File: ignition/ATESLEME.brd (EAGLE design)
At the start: 34.6 x 56.6 mm, 54 parts, among them U1 ADXL345PATRICK, U3 AMS1117-3.3

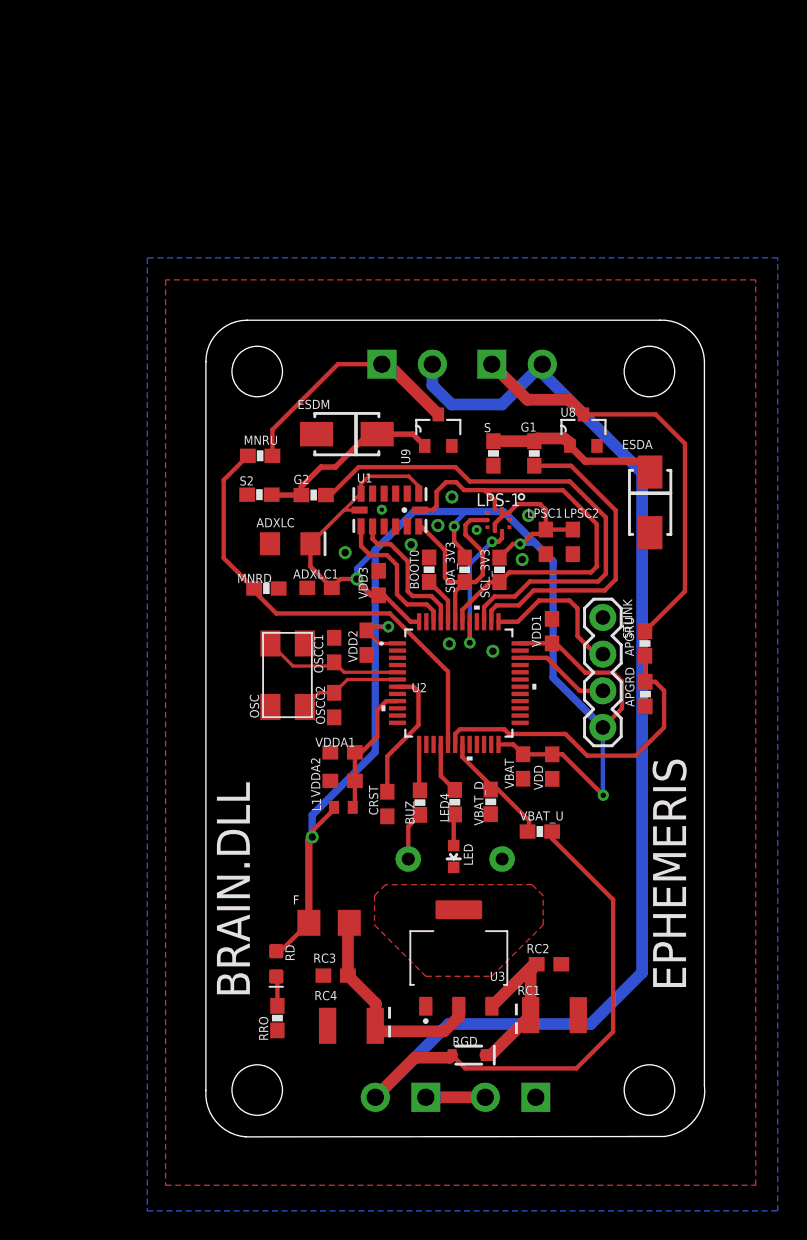
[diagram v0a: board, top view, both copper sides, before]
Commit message: Extra polygon was added for methal distance
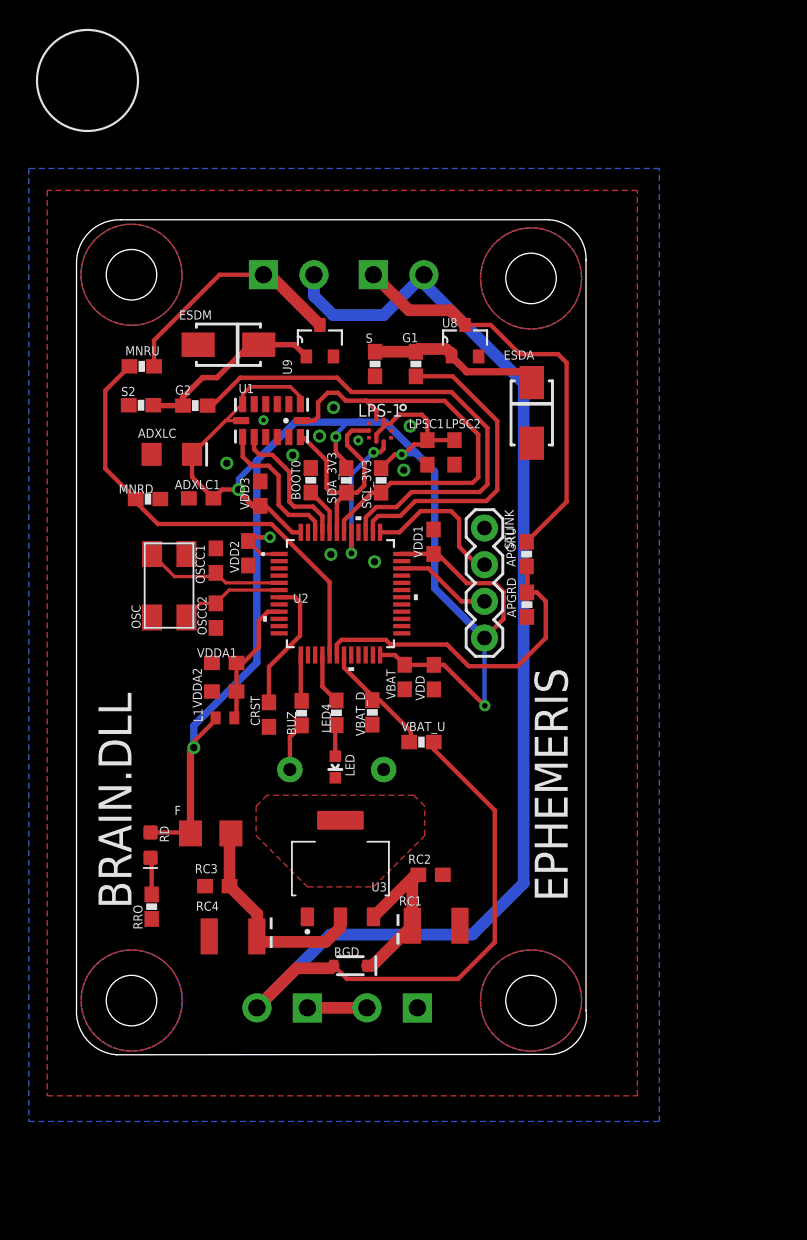
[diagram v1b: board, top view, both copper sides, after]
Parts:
- moved RD 12.0 mm to (-1.04, 21.0)
- moved RRO 11.6 mm to (-0.97, 16.8)
- moved APGRD 10.3 mm to (25.0, 37.7)
- moved ADXLC1 10.3 mm to (2.46, 45.1)
- moved APGRU 10.3 mm to (25.0, 41.2)
- moved APOGEE 10.3 mm to (14.4, 60.6)
- moved BUZ 10.3 mm to (9.42, 30.2)
- moved ESDA 10.3 mm to (25.4, 51.0)
- moved ESDM 10.3 mm to (4.36, 55.7)
- moved F 10.3 mm to (3.12, 21.8)
- moved G1 10.3 mm to (17.3, 54.4)
- moved LED 10.3 mm to (11.8, 26.4)
- moved LED4 10.3 mm to (11.8, 30.2)
- moved LPSC1 10.3 mm to (18.1, 48.2)
- moved LPSC2 10.3 mm to (20.0, 48.2)
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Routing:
- net N$2: track 2.06 -> 2.57 mm
- added copper zone on layer 1, net D
- added copper zone on layer 16, net D
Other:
- board size 34.6 x 56.6 mm -> 35.3 x 57.9 mm

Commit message: Redesign was maken for ignition
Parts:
- removed OSC: (no value), ABMM2-8.000MHZ-E2-T:ABMM2-8.000MHZ-E2-T
- added Y2: ABM2B-8.000MHZ-10-1-U-T, ABM3B-26.000MHZ-10-1-U-T:OSCCC500X320X110-4N
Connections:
- net GND: now also Y2.2, Y2.4
- net OSC_OUT: now also Y2.3; no longer OSC.OUT
- net OSC_ıN: now also Y2.1; no longer OSC.ıN
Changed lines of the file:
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@@
 <drawing>
 <settings>
-<setting alwaysvectorfont="yes"/>
+<setting alwaysvectorfont="no"/>
 <setting verticaltext="up"/>
 </settings>
@@
 <layer number="56" name="wert" color="7" fill="1" visible="no" active="no"/>
 <layer number="57" name="tCAD" color="7" fill="1" visible="no" active="no"/>
+<layer number="58" name="bCAD" color="11" fill="1" visible="no" active="no"/>
 <layer number="59" name="tCarbon" color="7" fill="1" visible="no" active="no"/>
 <layer number="60" name="bCarbon" color="7" fill="1" visible="no" active="no"/>
@@
 <attribute name="VALUE" x="-1.651" y="53.0606" size="0.635" layer="27" font="vector" ratio="15"/>
 </element>
-<element name="OSC" library="ABMM2-8.000MHZ-E2-T" package="ABMM2-8.000MHZ-E2-T" value="" x="0.1778" y="38.9636" smashed="yes" rot="R90">
-<attribute name="NAME" x="-1.7272" y="36.0172" size="0.635" layer="25" font="vector" ratio="15" rot="R90"/>
-<attribute name="VALUE" x="3.302" y="36.0172" size="0.762" layer="27" rot="R90"/>
-</element>
 <element name="OSCC1" library="SparkFun-Capacitors" library_urn="urn:adsk.eagle:library:510" package="0603" package3d_urn="urn:adsk.eagle:package:37414/1" value="25pF" x="3.4798" y="40.7416" smashed="yes" rot="R90">
 <attribute name="NAME" x="2.7178" y="40.4876" size="0.635" layer="25" font="vector" ratio="15" rot="R90" align="bottom-center"/>
@@
 <attribute name="PRICE" value="None" x="12.1158" y="19.4056" size="1.778" layer="27" display="off"/>
 <attribute name="VALUE" x="8.419240625" y="21.87065" size="0.635" layer="27" font="vector" ratio="15"/>
+</element>
+<element name="Y2" library="ABM3B-26.000MHZ-10-1-U-T" package="OSCCC500X320X110-4N" value="ABM2B-8.000MHZ-10-1-U-T" x="0.254" y="38.8366" smashed="yes" rot="R270">
+<attribute name="AVAILABILITY" value="Good" x="8.9916" y="46.8884" size="1.778" layer="27" rot="R270" display="off"/>
+<attribute name="DESCRIPTION" value=" 26MHz ±10ppm Crystal 10pF 50 Ohms 4-SMD, No Lead " x="8.9916" y="46.8884" size="1.778" layer="27" rot="R270" display="off"/>
+<attribute name="MF" value="Abracon" x="8.9916" y="46.8884" size="1.778" layer="27" rot="R270" display="off"/>
+<attribute name="MP" value="ABM3B-26.000MHZ-10-1-U-T" x="8.9916" y="46.8884" size="1.778" layer="27" rot="R270" display="off"/>
+<attribute name="NAME" x="2.79841875" y="41.38101875" size="1.272209375" layer="25" rot="R270"/>
+<attribute name="PACKAGE" value="SMD-4 Abracon LLC" x="8.9916" y="46.8884" size="1.778" layer="27" rot="R270" display="off"/>
+<attribute name="PRICE" value="None" x="8.9916" y="46.8884" size="1.778" layer="27" rot="R270" display="off"/>
+<attribute name="PURCHASE-URL" value="https://pricing.snapeda.com/search/part/ABM3B-26.000MHZ-10-1-U-T/?ref=eda" x="8.9916" y="46.8884" size="1.778" layer="27" rot="R270" display="off"/>
+<attribute name="VALUE" x="-3.56321875" y="41.381409375" size="1.272409375" layer="27" rot="R270"/>
 </element>
 </elements>
@@
 <via x="6.7818" y="50.4698" extent="1-16" drill="0.3048"/>
 <via x="4.2418" y="47.498" extent="1-16" drill="0.508"/>
+<contactref element="Y2" pad="4"/>
+<contactref element="Y2" pad="2"/>
 </signal>
 <signal name="VCC">
@@
 <wire x1="8.7811" y1="42.7056" x2="6.951978125" y2="44.534721875" width="0.3048" layer="1"/>
 <wire x1="6.951978125" y1="44.534721875" x2="6.5659" y2="44.534721875" width="0.3048" layer="1"/>
-<wire x1="7.8658" y1="41.2056" x2="6.629315625" y2="41.2056" width="0.2286" layer="1"/>
-<wire x1="6.629315625" y1="41.2056" x2="5.7302375" y2="42.104678125" width="0.2286" layer="1"/>
+<wire x1="7.8658" y1="41.2056" x2="6.629315625" y2="41.2056" width="0.3048" layer="1"/>
+<wire x1="6.629315625" y1="41.2056" x2="5.7302375" y2="42.104678125" width="0.3048" layer="1"/>
 <wire x1="15.12061875" y1="50.20614375" x2="15.56904375" y2="50.20614375" width="0.3048" layer="1"/>
 <wire x1="15.56904375" y1="50.20614375" x2="15.6215" y2="50.2586" width="0.1524" layer="1"/>
@@
 <signal name="OSC_ıN">
 <contactref element="U2" pad="5"/>
-<contactref element="OSC" pad="ıN"/>
 <contactref element="OSCC1" pad="1"/>
-<wire x1="-0.9398" y1="41.1988" x2="0.6214" y2="39.6376" width="0.2286" layer="1"/>
-<wire x1="3.2258" y1="39.6376" x2="0.6214" y2="39.6376" width="0.2286" layer="1"/>
-<wire x1="3.2258" y1="39.6376" x2="3.4798" y2="39.8916" width="0.2286" layer="1"/>
-<wire x1="7.8658" y1="39.2056" x2="4.1658" y2="39.2056" width="0.2286" layer="1"/>
-<wire x1="4.1658" y1="39.2056" x2="3.4798" y2="39.8916" width="0.2286" layer="1"/>
+<wire x1="7.8658" y1="39.2056" x2="4.1658" y2="39.2056" width="0.3048" layer="1"/>
+<wire x1="4.1658" y1="39.2056" x2="3.5755" y2="39.7959" width="0.3048" layer="1"/>
+<contactref element="Y2" pad="1"/>
+<wire x1="3.5755" y1="39.7959" x2="3.4798" y2="39.8916" width="0.2286" layer="1"/>
+<wire x1="-0.946" y1="41.0366" x2="0.619" y2="39.4716" width="0.3048" layer="1"/>
+<wire x1="3.2512" y1="39.4716" x2="3.5755" y2="39.7959" width="0.3048" layer="1"/>
+<wire x1="0.619" y1="39.4716" x2="3.2512" y2="39.4716" width="0.3048" layer="1"/>
 </signal>
 <signal name="OSC_OUT">
 <contactref element="U2" pad="6"/>
-<contactref element="OSC" pad="OUT"/>
 <contactref element="OSCC2" pad="1"/>
-<wire x1="1.4478" y1="36.8046" x2="2.4248" y2="37.7816" width="0.2286" layer="1"/>
-<wire x1="2.4248" y1="37.7816" x2="3.4798" y2="37.7816" width="0.2286" layer="1"/>
-<wire x1="7.8658" y1="38.7056" x2="4.4038" y2="38.7056" width="0.2286" layer="1"/>
-<wire x1="4.4038" y1="38.7056" x2="3.4798" y2="37.7816" width="0.2286" layer="1"/>
+<wire x1="7.8658" y1="38.7056" x2="4.4038" y2="38.7056" width="0.3048" layer="1"/>
+<wire x1="4.4038" y1="38.7056" x2="3.4798" y2="37.7816" width="0.3048" layer="1"/>
+<contactref element="Y2" pad="3"/>
+<wire x1="1.454" y1="36.6366" x2="2.599" y2="37.7816" width="0.3048" layer="1"/>
+<wire x1="2.599" y1="37.7816" x2="3.4798" y2="37.7816" width="0.3048" layer="1"/>
 </signal>
 <signal name="PC13">
